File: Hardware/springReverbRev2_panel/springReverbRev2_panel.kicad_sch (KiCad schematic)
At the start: 21 parts

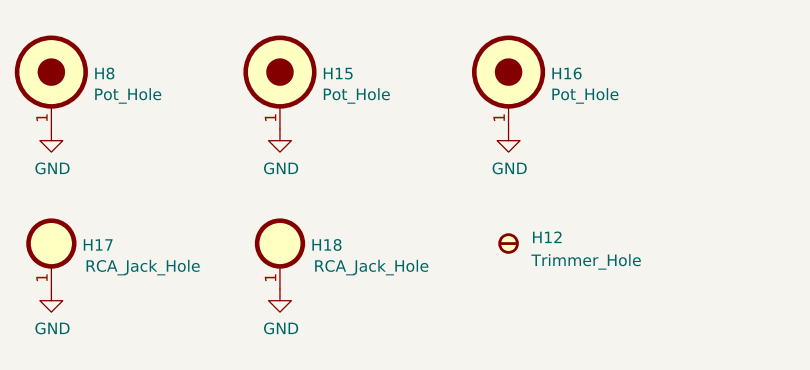
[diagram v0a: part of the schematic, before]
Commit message: Ungrounded jack for tank send
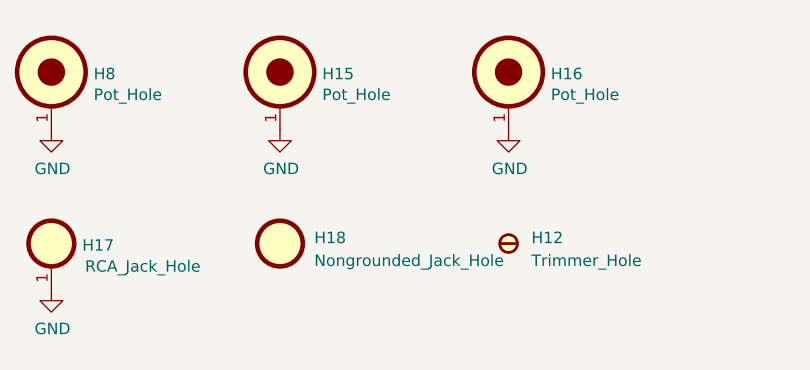
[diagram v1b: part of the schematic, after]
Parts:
- removed H18: RCA_Jack_Hole, springReverbRev2_panel:Kosmo_RCA_Jack_Hole, symbol springReverbRev2_panel:RCA_Jack_Hole
- added H18: Nongrounded_Jack_Hole, springReverbRev2_panel:Kosmo_Nongrounded_RCA_Jack_Hole, symbol springReverbRev2_panel:Nongrounded_Jack_Hole
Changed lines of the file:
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@@
     )
   )
-  (symbol (lib_id "springReverbRev2_panel:RCA_Jack_Hole") (at 127 114.3 0) (unit 1)
-    (in_bom no) (on_board yes) (dnp no)
-    (property "Reference" "H18" (at 130.429 114.5032 0)
+  (symbol (lib_id "springReverbRev2_panel:Nongrounded_Jack_Hole") (at 127 114.3 0) (unit 1)
+    (in_bom yes) (on_board yes) (dnp no) (fields_autoplaced)
+    (property "Reference" "H18" (at 130.81 113.665 0)
       (effects (font (size 1.27 1.27)) (justify left))
     )
-    (property "Value" "RCA_Jack_Hole" (at 137.16 116.84 0)
-      (effects (font (size 1.27 1.27)))
+    (property "Value" "Nongrounded_Jack_Hole" (at 130.81 116.205 0)
+      (effects (font (size 1.27 1.27)) (justify left))
     )
-    (property "Footprint" "springReverbRev2_panel:Kosmo_RCA_Jack_Hole" (at 127 110.49 0)
+    (property "Footprint" "springReverbRev2_panel:Kosmo_Nongrounded_RCA_Jack_Hole" (at 127 110.49 0)
       (effects (font (size 1.27 1.27)) hide)
     )
@@
       (effects (font (size 1.27 1.27)) hide)
     )
-    (pin "1")
     (instances
       (project "springReverbRev2_panel"
@@
         )
       )
-    )
-  )
-  (symbol (lib_id "power:GND") (at 127 119.38 0) (unit 1)
-    (in_bom yes) (on_board yes) (dnp no)
-    (property "Reference" "#PWR017" (at 127 125.73 0)
-      (effects (font (size 1.27 1.27)) hide)
-    )
-    (property "Value" "GND" (at 127.127 123.7742 0)
-      (effects (font (size 1.27 1.27)))
-    )
-    (property "Footprint" "" (at 127 119.38 0)
-      (effects (font (size 1.27 1.27)) hide)
-    )
-    (property "Datasheet" "" (at 127 119.38 0)
-      (effects (font (size 1.27 1.27)) hide)
-    )
-    (pin "1")
-    (instances
-      (project "springReverbRev2_panel"
-        (path "/51ee3bd4-7fc3-45ce-b924-e23131ebd243"
-          (reference "#PWR017") (unit 1)
-        )
-      )
